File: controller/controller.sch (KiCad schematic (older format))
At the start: 18 parts, among them J1 USB_B_Micro, SW1 SW_RESET, U1 ATmega32U4-AU, X1 XTAL

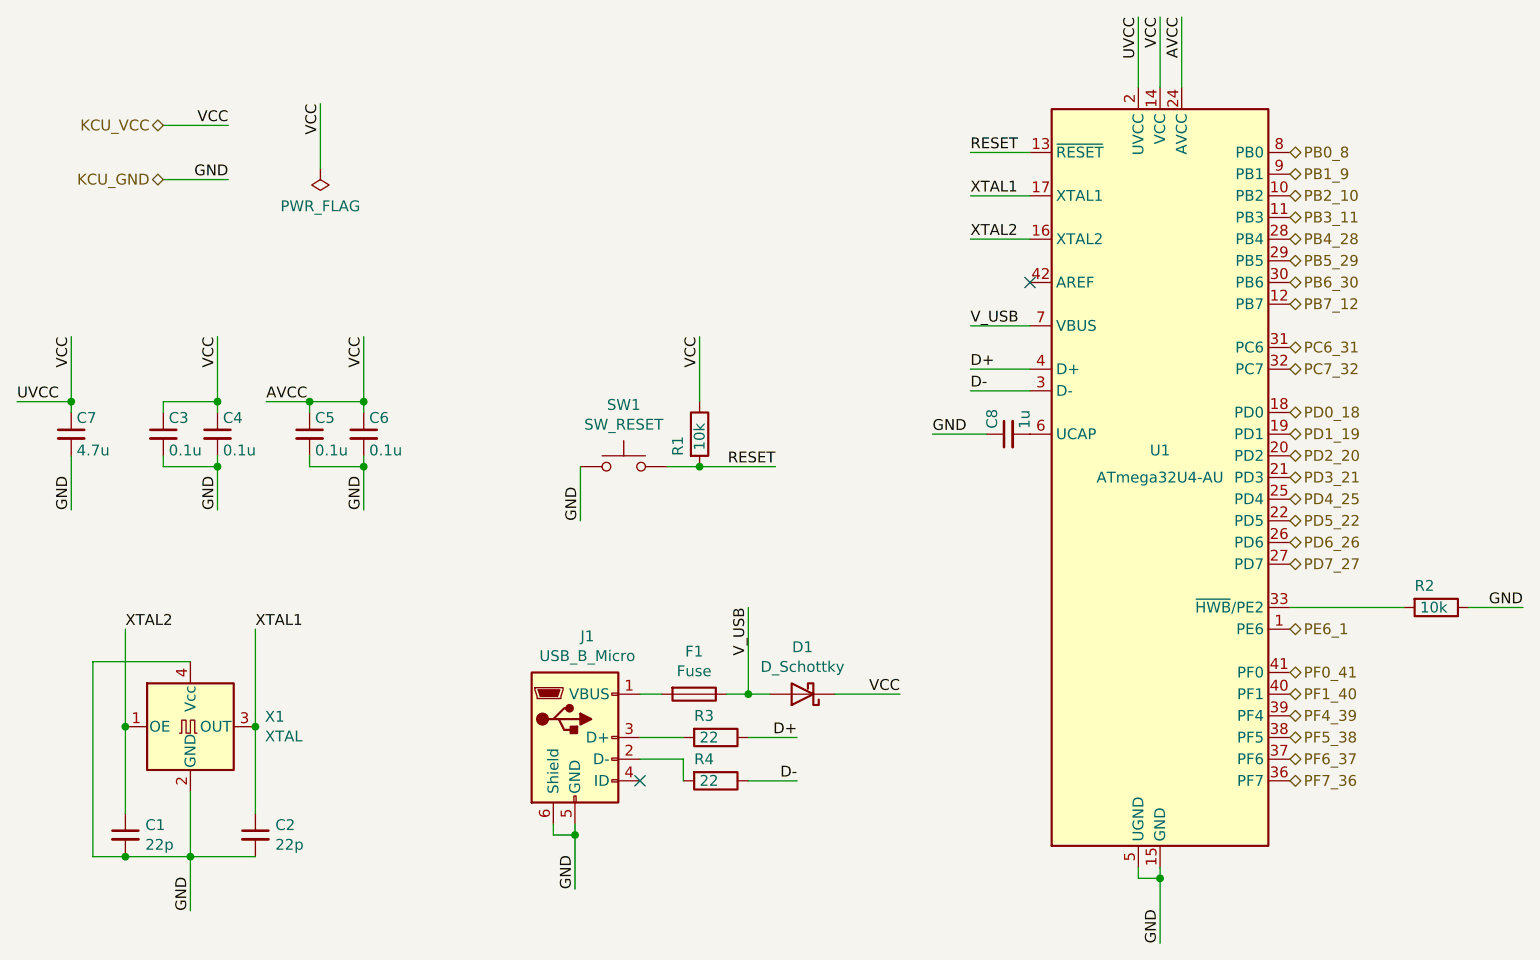
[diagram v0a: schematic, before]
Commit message: controller: fill footprints
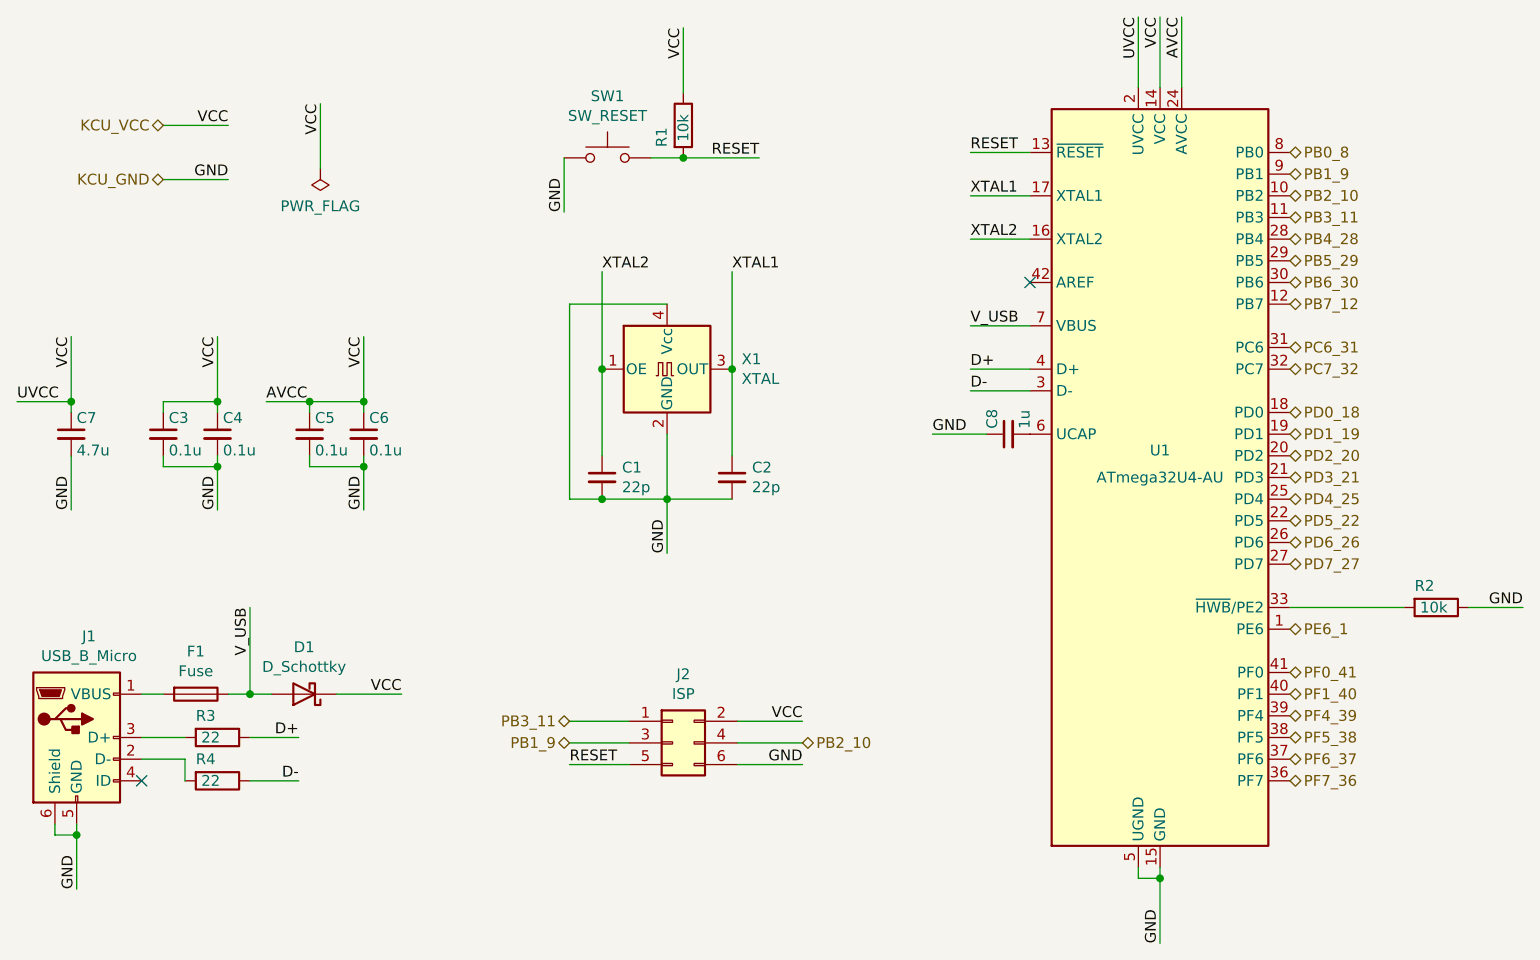
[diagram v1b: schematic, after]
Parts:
- added J2: ISP, Connector_PinHeader_2.54mm:PinHeader_2x03_P2.54mm_Vertical, symbol Connector_Generic:Conn_02x03_Odd_Even
- C1, C2, C3, C4, C5, C6, C7, C8: footprint (none) -> Capacitor_SMD:C_0603_1608Metric_Pad1.08x0.95mm_HandSolder
- D1: footprint (none) -> Diode_SMD:D_SOD-123
- F1: footprint (none) -> Fuse:Fuse_1206_3216Metric_Pad1.42x1.75mm_HandSolder
- J1: footprint (none) -> KeyboardController:USB-MicroB_ZX62M-B-5P
- R1, R2, R3, R4: footprint (none) -> Resistor_SMD:R_0603_1608Metric_Pad0.98x0.95mm_HandSolder
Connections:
- net KCU_GND: now also J2.6 (Pin_6)
- net KCU_VCC: now also J2.2 (Pin_2)
- net PB1_9: now also J2.3 (Pin_3)
- net PB2_10: now also J2.4 (Pin_4)
- net PB3_11: now also J2.1 (Pin_1)
- net RESET: now also J2.5 (Pin_5)
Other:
- moved on the sheet: C1, C2, D1, F1, J1, R1, R3, R4, SW1, X1
